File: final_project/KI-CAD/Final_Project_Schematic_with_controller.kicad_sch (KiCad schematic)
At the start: 33 parts, among them P1 Wall_Wart_Plug, SW1 Power Button, SW2 RPG 1, SW3 RPG 2, SW4 Home Button, SW5 Up Arrow Button, SW6 Down Arrow Button, U1 ATmega328P, U2 ESP32-C3-WROOM-02, U3 Bi-Directional Logic Converter, U4 LED MATRIX

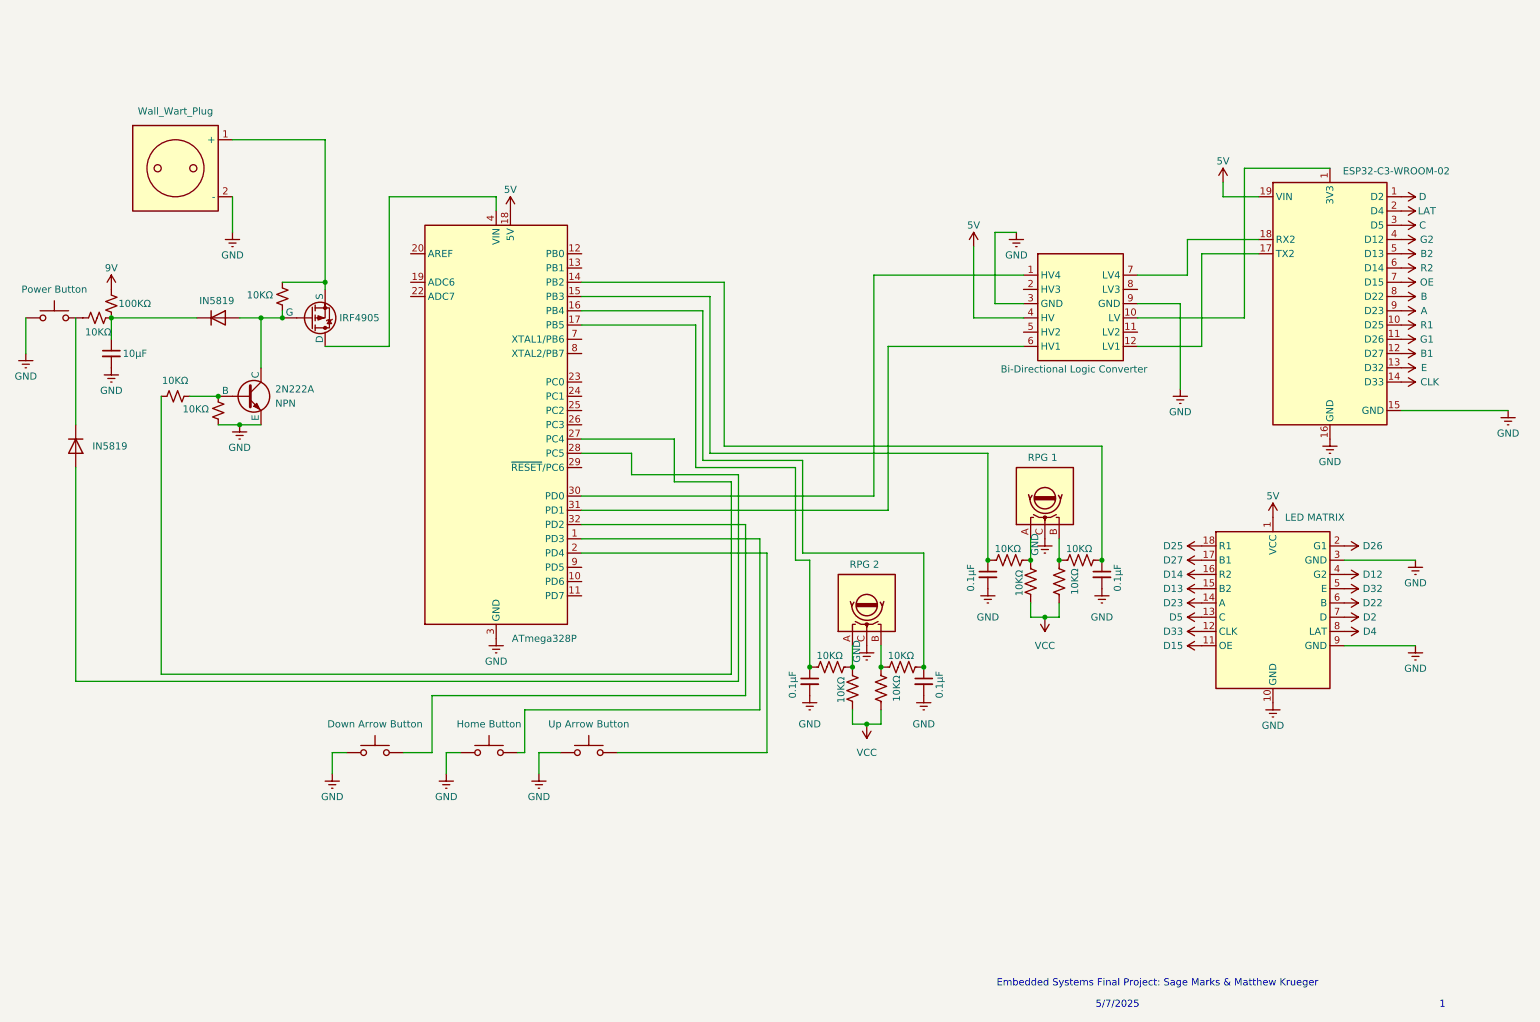
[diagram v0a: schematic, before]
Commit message: schematics are done, one with controllers, one without
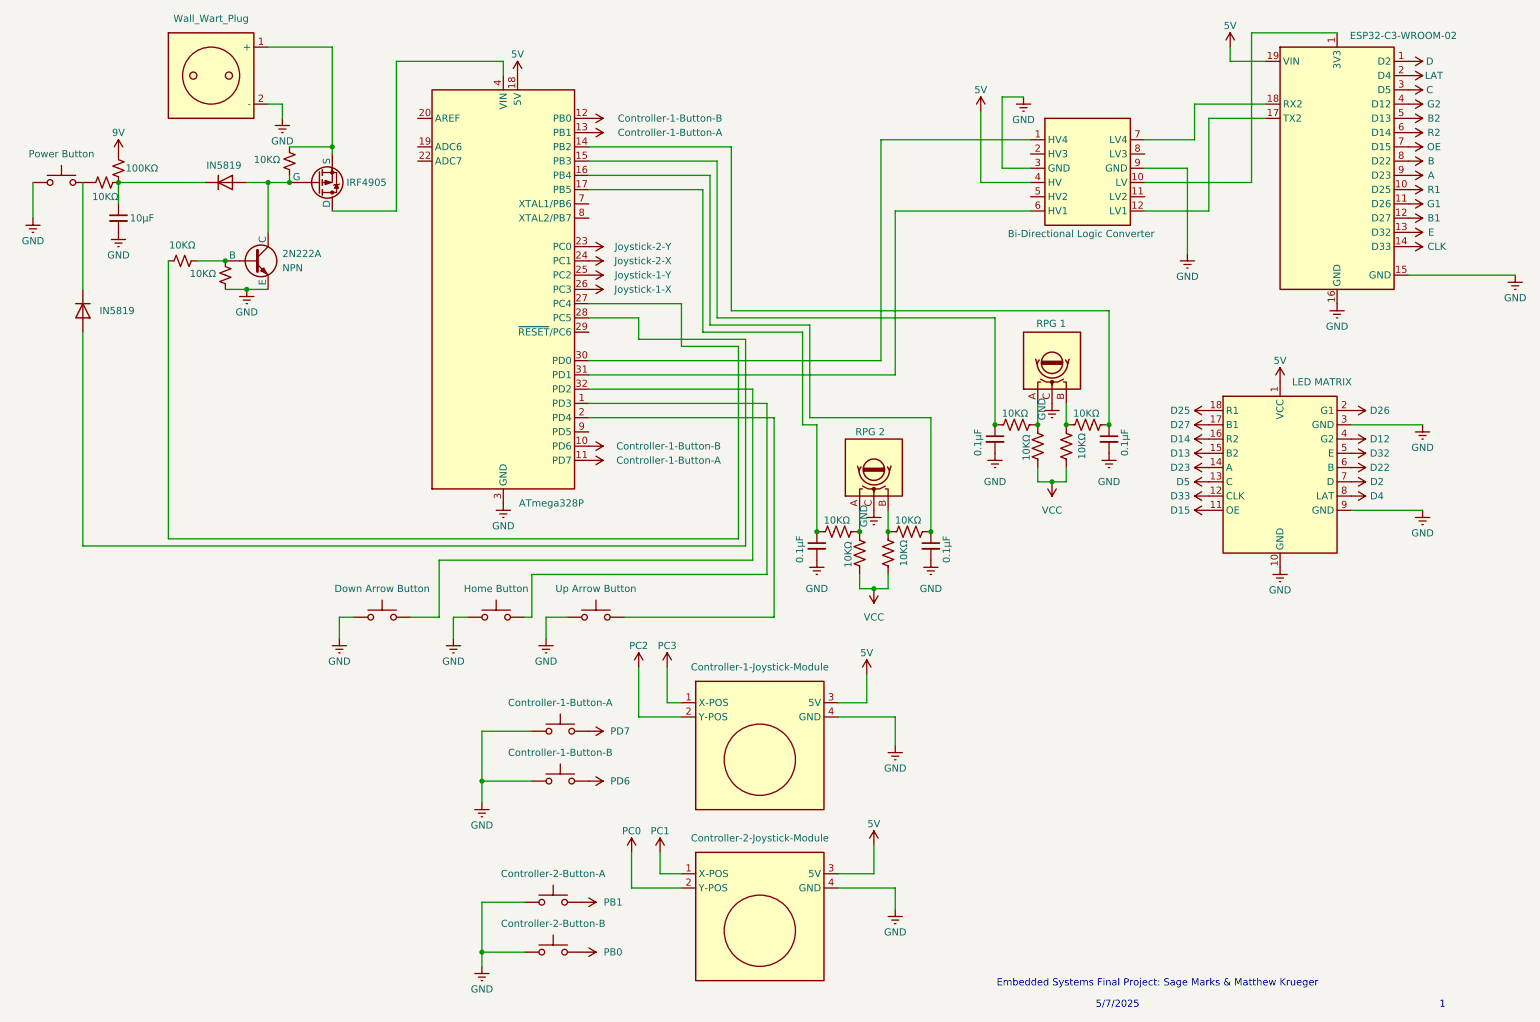
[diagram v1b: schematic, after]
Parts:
- added A1: Controller-1-Joystick-Module, Module:Arduino_Nano, symbol MCU_Module:Arduino_Nano_ESP32
- added A2: Controller-2-Joystick-Module, Module:Arduino_Nano, symbol MCU_Module:Arduino_Nano_ESP32
- added SW10: Controller-2-Button-B, symbol Switch:SW_Push
- added SW7: Controller-1-Button-A, symbol Switch:SW_Push
- added SW8: Controller-1-Button-B, symbol Switch:SW_Push
- added SW9: Controller-2-Button-A, symbol Switch:SW_Push
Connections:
- net 5V: now also A1.3 (5V), A2.3 (5V)
- net GND: now also A1.4 (GND), A2.4 (GND), SW10.1, SW7.1, SW8.1, SW9.1
- net Controller-1-Button-B: now reaches U1.10 (PD6)
- net Controller-1-Button-B: now also U1.12 (PB0)
- net Controller-1-Button-A: now reaches U1.11 (PD7)
- net Controller-1-Button-A: now also U1.13 (PB1)
- net Joystick-2-Y: now reaches U1.23 (PC0)
- net Joystick-2-X: now reaches U1.24 (PC1)
- net Joystick-1-Y: now reaches U1.25 (PC2)
- net Joystick-1-X: now reaches U1.26 (PC3)
- new net PB0: SW10.2
- new net PB1: SW9.2
- new net PC0: A2.2 (Y-POS)
- new net PC1: A2.1 (X-POS)
- new net PC2: A1.2 (Y-POS)
- new net PC3: A1.1 (X-POS)
- new net PD6: SW8.2
- new net PD7: SW7.2
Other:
- moved on the sheet: 100KΩ, 10KΩ, 2N222A, IRF4905
